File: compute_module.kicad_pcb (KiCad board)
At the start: 4 copper layers, 93.2 x 62.4 mm, 52 parts, among them J1 2001-1-2-21-00-BK, P1 POWER, P2 HOST, P3 CAM1, P4 CONN_02X20, Q1 2N7002P.215, Q2 DMP3056L-7, Q3 2N7002P.215, U1 REG1117-3.3, U3 REG1117A-1.8

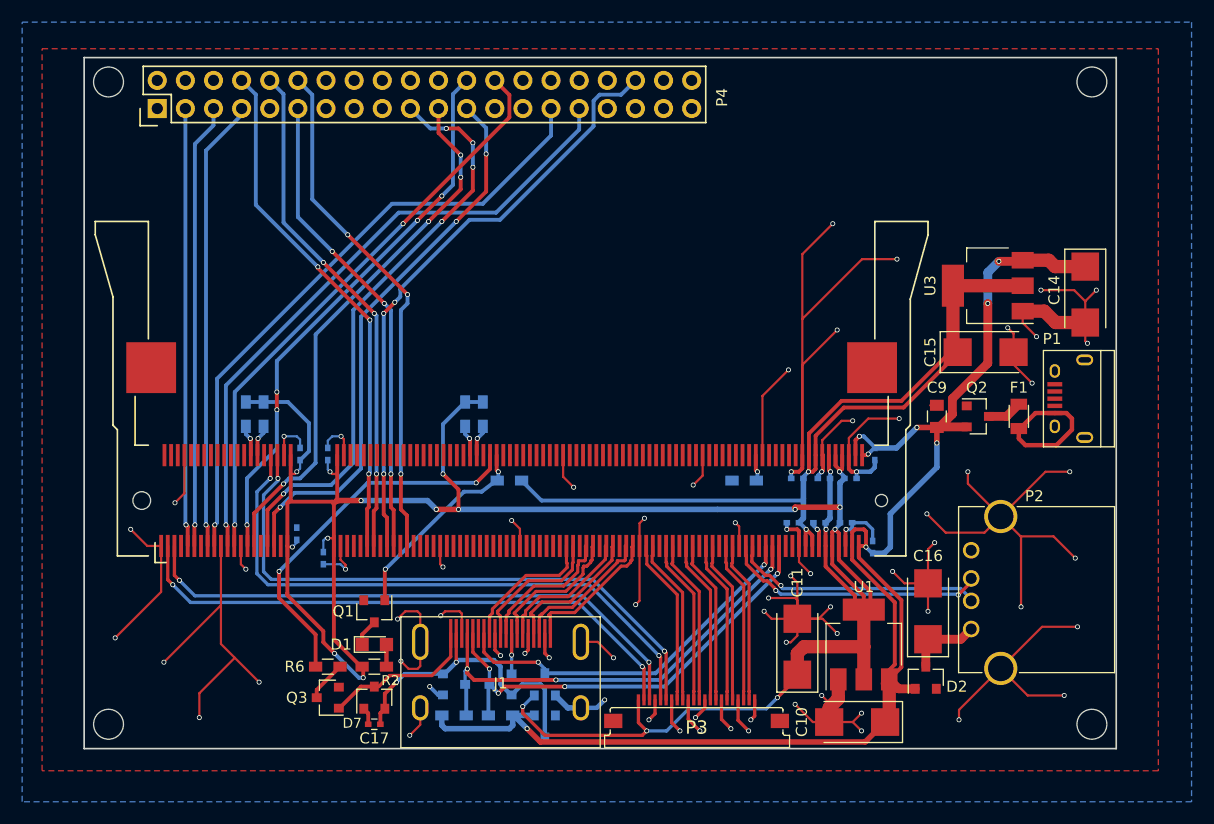
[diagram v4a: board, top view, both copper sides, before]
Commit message: Routed gpio header
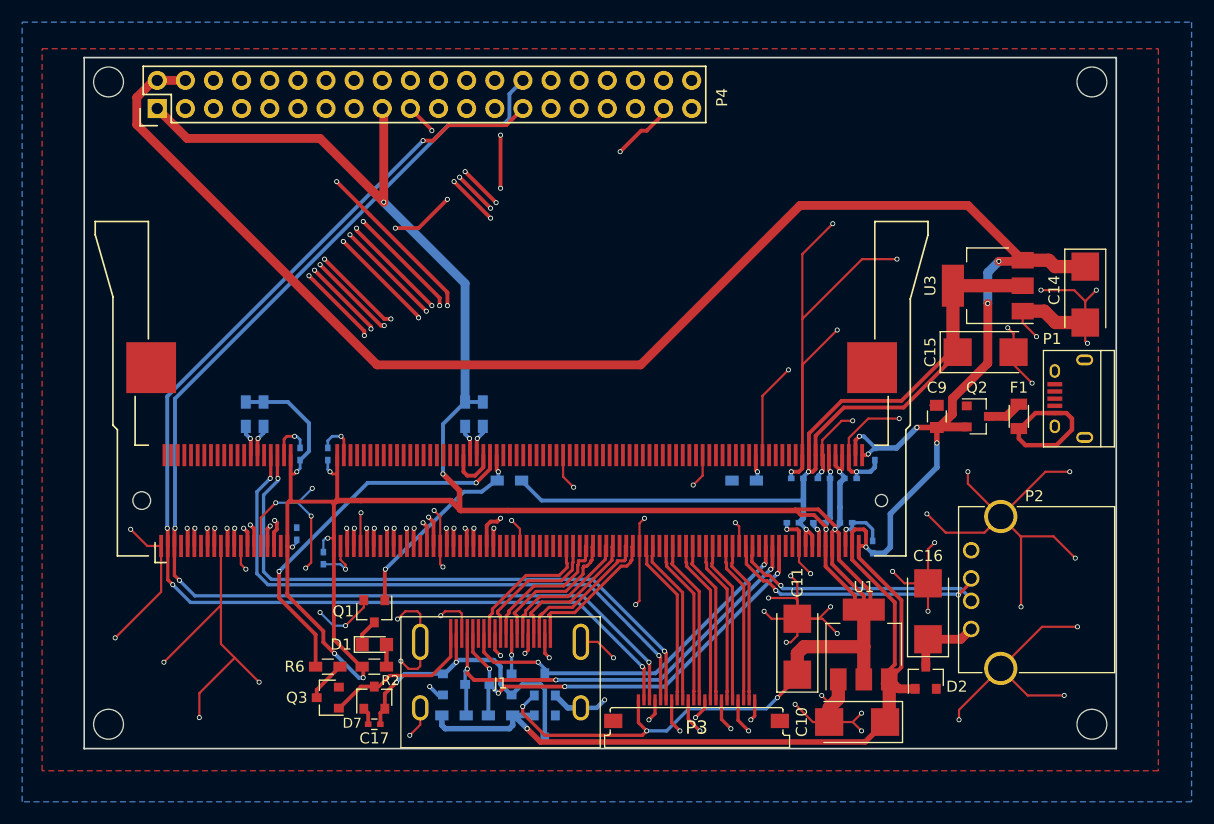
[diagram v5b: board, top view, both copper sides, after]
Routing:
- net +5V: track 141.0 -> 245.5 mm
- net GPIO21: track 0.00 -> 58.2 mm, vias 0 -> 1
- net CD1_SCL: track 52.2 -> 110.1 mm, vias 2 -> 3
- net +3V3: track 215.0 -> 272.8 mm, vias 19 -> 15
- net CD1_SDA: track 52.2 -> 108.6 mm, vias 2 -> 4
- net GPIO20: track 0.00 -> 56.2 mm, vias 0 -> 1
- net GPIO12: track 0.00 -> 54.8 mm, vias 0 -> 1
- net GPIO19: track 0.00 -> 52.3 mm, vias 0 -> 1
- net GPIO26: track 0.00 -> 51.9 mm, vias 0 -> 2
- net GPIO13: track 0.00 -> 51.9 mm, vias 0 -> 1
- net GPIO25: track 0.00 -> 49.5 mm, vias 0 -> 3
- net GPIO24: track 0.00 -> 48.4 mm, vias 0 -> 3
- net GPIO23: track 0.00 -> 47.1 mm, vias 0 -> 3
- net GPIO27: track 0.00 -> 45.8 mm, vias 0 -> 3
- net GPIO22: track 0.00 -> 43.8 mm, vias 0 -> 3
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
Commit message: Changed ground via size
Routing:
- net GND: track 392.9 -> 671.1 mm, vias 82 -> 120
- net +3V3: track 272.8 -> 361.5 mm, vias 15 -> 18
- net +1V8: track 88.6 -> 88.0 mm

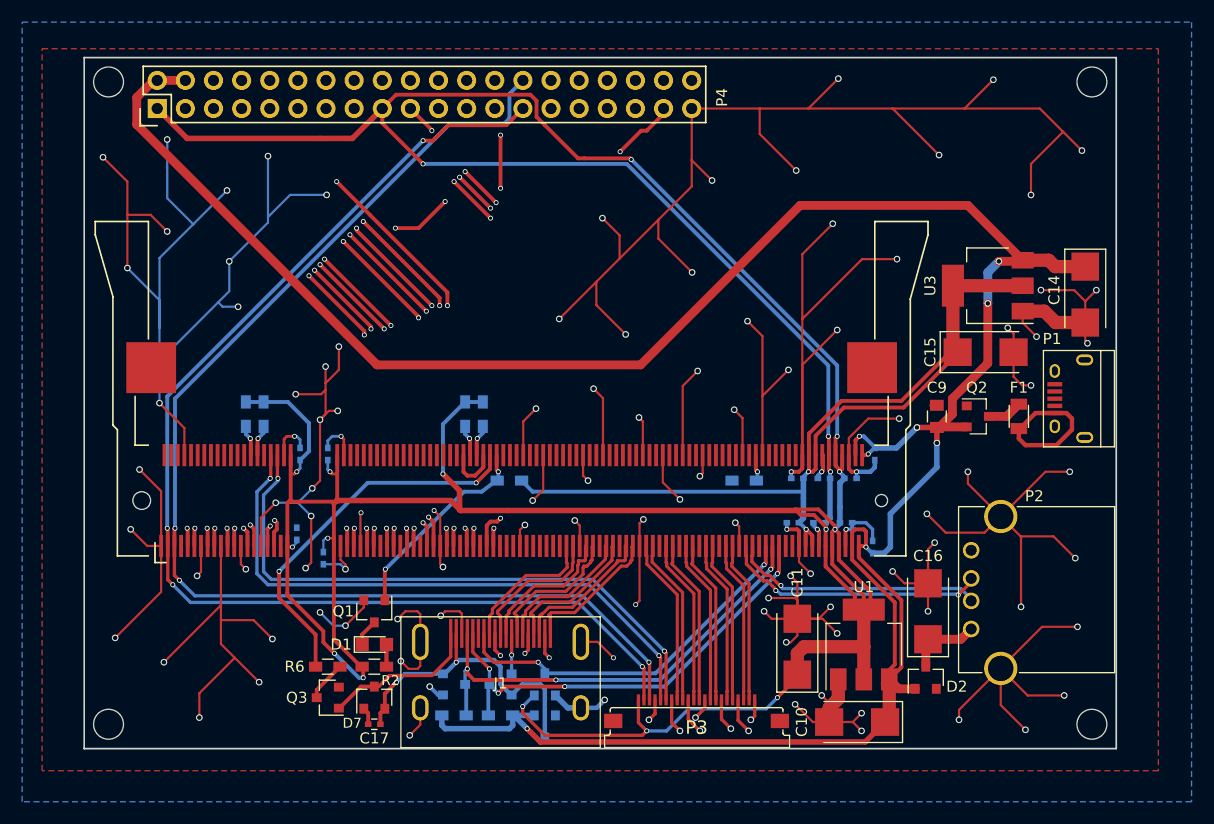
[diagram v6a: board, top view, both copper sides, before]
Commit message: Added labels on silkscreen
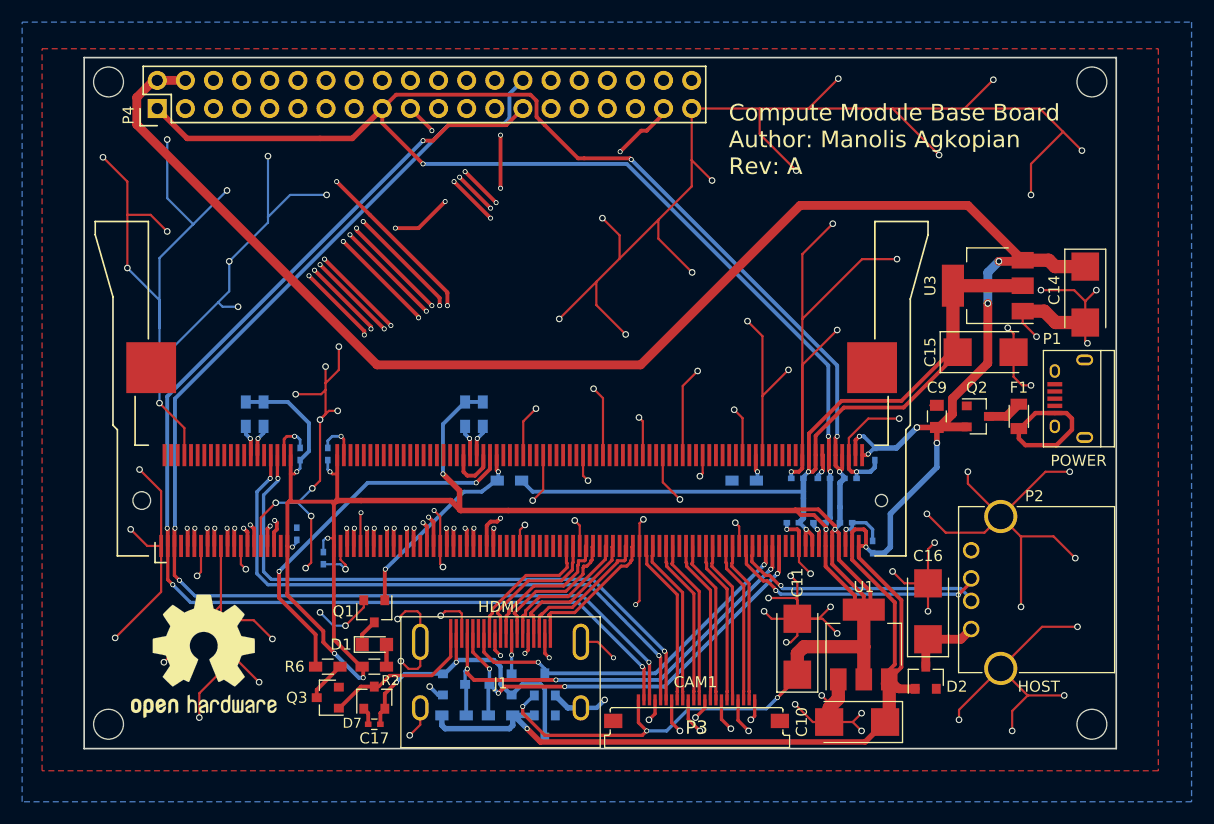
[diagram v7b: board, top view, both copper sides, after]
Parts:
- added REF***: OSHW-Logo2_14.6x12mm_SilkScreen, Symbols:OSHW-Logo2_14.6x12mm_SilkScreen, F.Cu at (98.4, 98.0)
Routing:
- net GND: track 671.1 -> 668.4 mm
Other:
- board text added: "CAM1"
- board text added: "Compute Module Base Board Author: Manolis Agkopian Rev: A"
- board text added: "HDMI"
- board text added: "HOST"
- board text added: "POWER"

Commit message: Minor fixes and rounded board edges
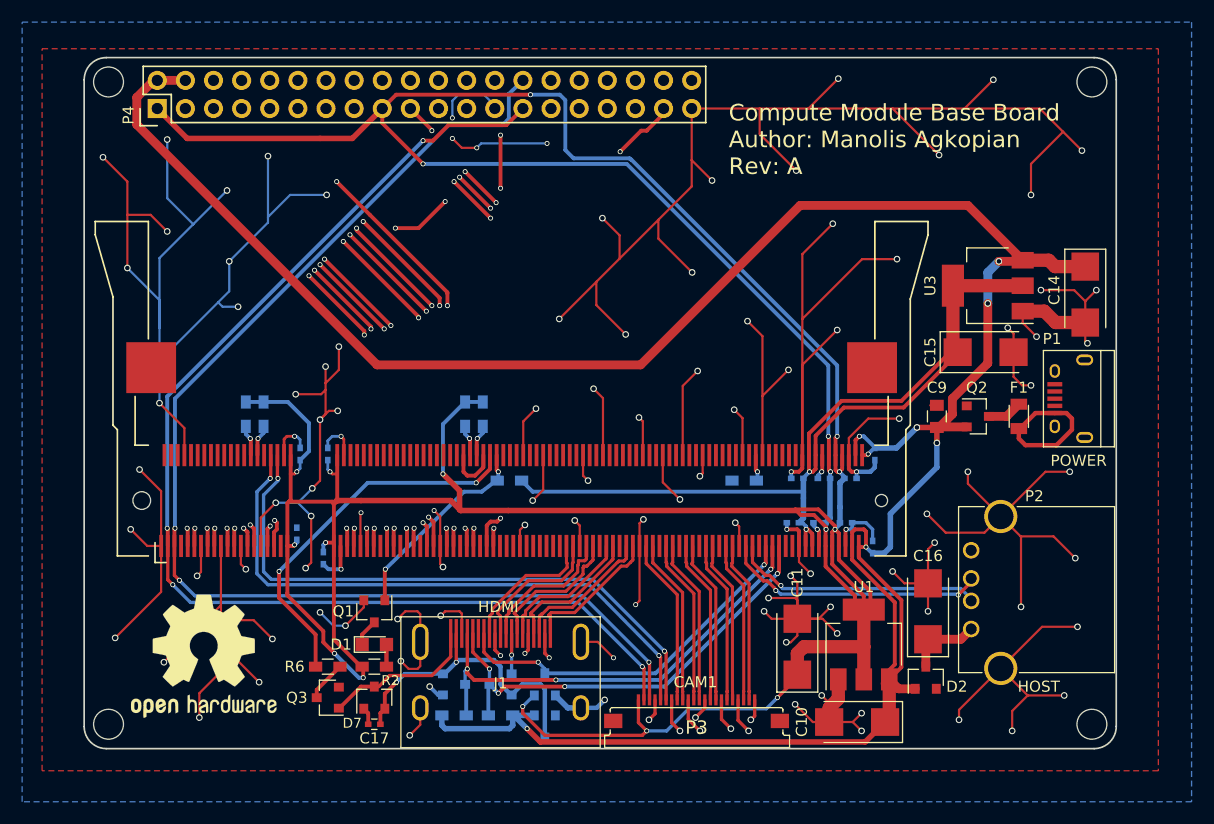
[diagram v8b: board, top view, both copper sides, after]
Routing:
- net GND: track 668.4 -> 684.9 mm, vias 120 -> 124
- net +3V3: track 361.5 -> 362.7 mm
- net CAM1_D3_P: track 15.1 -> 15.9 mm
- net USB_D_P: track 24.0 -> 24.8 mm
- net USB_D_N: track 22.9 -> 23.7 mm
- net CAM1_D3_N: track 15.1 -> 15.8 mm
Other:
- outline, holes or cut-outs redrawn
